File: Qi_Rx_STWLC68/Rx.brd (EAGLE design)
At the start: 160 x 100 mm, 44 parts, among them IC1 STWLC68JRH

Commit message: Complete SMD layout
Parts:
- moved R3 44.7 mm to (11.4, 15.2)
- moved R4 43.7 mm to (15.2, 15.2)
- moved R5 42.7 mm to (19.1, 15.2)
- moved C11 40.7 mm to (34.3, 19.1)
- moved C7 40.7 mm to (39.4, 12.7)
- moved C8 40.7 mm to (34.3, 12.7)
- moved C9 40.7 mm to (39.4, 19.1)
- moved U$2 40.7 mm to (48.3, 21.6)
- moved C1 40.7 mm to (39.4, 8.89)
- moved C10 40.7 mm to (36.8, 19.1)
- moved C12 40.7 mm to (43.2, 26.7)
- moved C13 40.7 mm to (25.4, 8.89)
- moved C14 40.7 mm to (22.9, 8.89)
- moved C15 40.7 mm to (40.6, 26.7)
- moved C17 40.7 mm to (35.6, 26.7)
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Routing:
- net VOUT: track 14.1 -> 37.1 mm
- net SDA: track 29.9 -> 33.7 mm
- net INT: track 27.1 -> 29.6 mm
- net GND: vias 0 -> 21
- added copper zone on layer 1, net GND
- added copper zone on layer 15, net GND
- added copper zone on layer 16, net GND
- added copper zone on layer 2, net GND
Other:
- board size 160 x 100 mm -> 68.6 x 38.1 mm

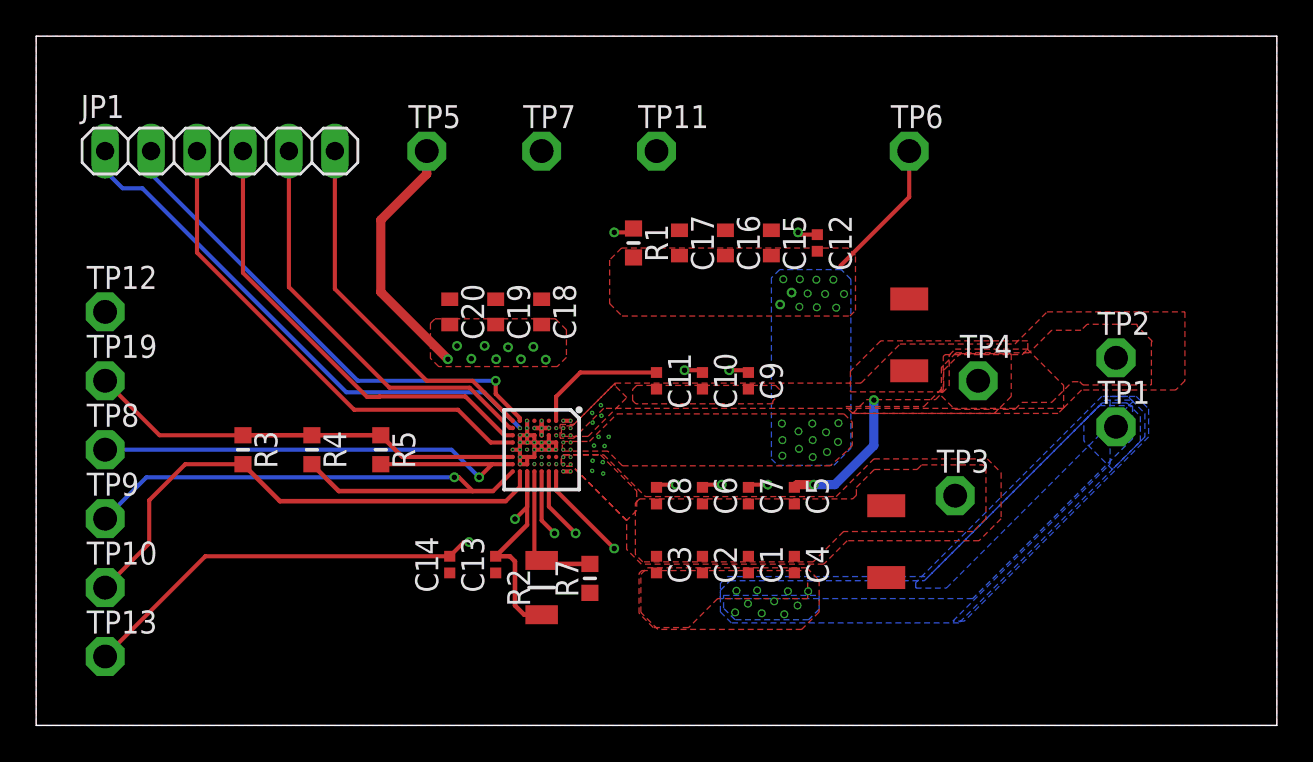
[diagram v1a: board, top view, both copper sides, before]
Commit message: Rx surface-mount cleanup
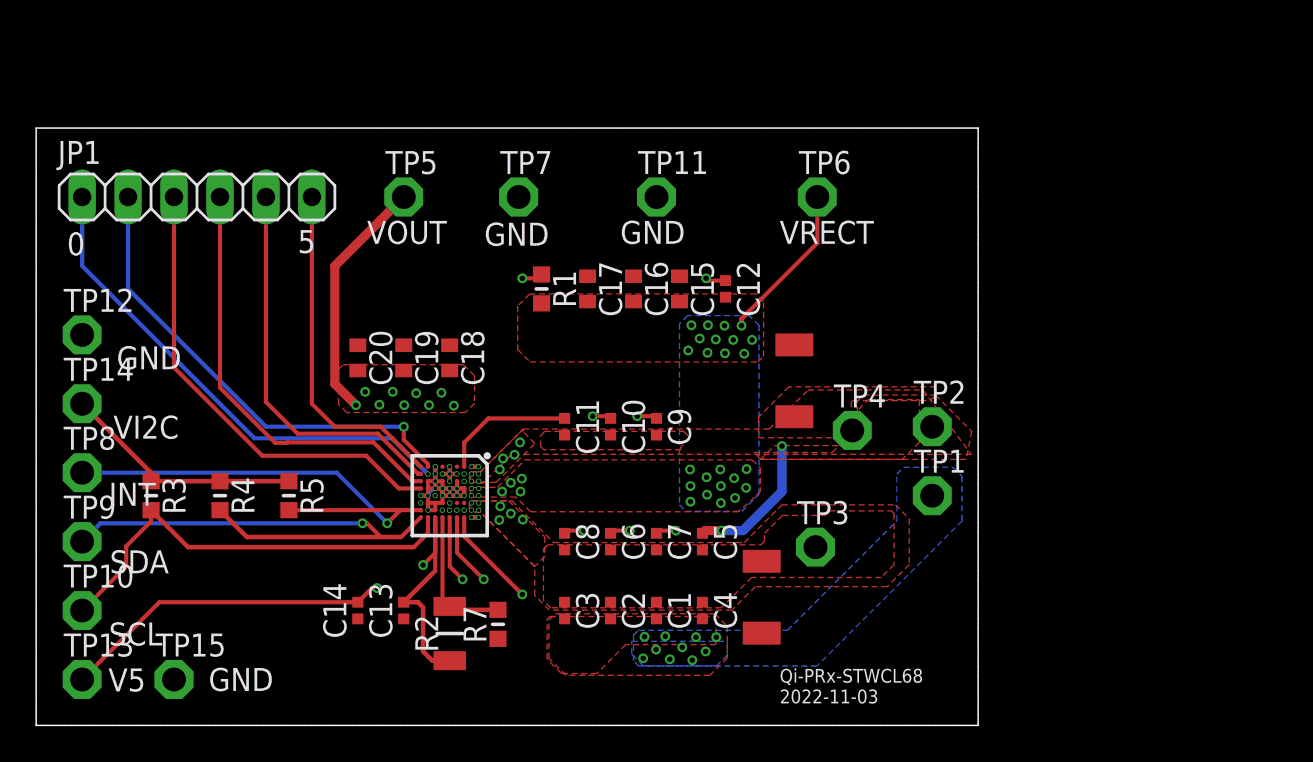
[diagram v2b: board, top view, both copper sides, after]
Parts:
- removed TP19: PTR1PAD1-13, testpad:P1-13
- added TP14, TP15: TPPAD1-13, testpad:P1-13
- moved TP1 10.9 mm to (49.5, 12.7)
- moved TP2 10.9 mm to (49.5, 16.5)
- moved TP3 8.23 mm to (43.1, 9.86)
- moved U$1 7.54 mm to (40.1, 7.09)
- moved TP4 7.48 mm to (45.1, 16.3)
- moved U$2 6.84 mm to (41.9, 19.1)
- moved C17 5.68 mm to (30.5, 24.1)
- moved R1 5.68 mm to (27.9, 24.1)
- moved IC1 5.68 mm to (22.9, 12.7)
- moved C18 5.68 mm to (22.9, 20.3)
- moved R2 5.68 mm to (22.9, 5.08)
- moved R3 5.68 mm to (6.35, 12.7)
- moved R4 5.68 mm to (10.2, 12.7)
- moved R5 5.68 mm to (14.0, 12.7)
- moved C1 5.68 mm to (34.3, 6.35)
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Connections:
- new net VI2C: R3.2, R4.2, R5.2, TP14.TP
- net GND: now also TP15.TP
- net V18: no longer R3.2, R4.2, R5.2, TP19.TP
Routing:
- net V18: track 42.0 -> 19.7 mm, vias 2 -> 3
- net GND: track 12.4 -> 30.1 mm, vias 21 -> 18
- net VI2C: track 0.00 -> 13.5 mm
- net SCL: track 29.2 -> 24.5 mm
- net SDA: track 33.7 -> 29.4 mm
- net V5: track 30.8 -> 26.5 mm
- net INT: track 29.6 -> 26.3 mm
- net GPIO0: track 29.9 -> 27.7 mm
- net VOUT: track 37.1 -> 39.2 mm
- net GPIO5: track 20.5 -> 18.9 mm
- net GPIO1: track 27.8 -> 26.2 mm
- net GPIO4: track 23.1 -> 21.5 mm
- net GPIO3: track 25.4 -> 23.8 mm
- net GPIO2: track 27.4 -> 25.8 mm
- net VRECT: track 8.54 -> 9.50 mm
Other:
- board size 68.6 x 38.1 mm -> 52.1 x 33 mm
- board text added: "0"
- board text added: "5"
- board text added: "GND"
- board text added: "INT"
- board text added: "Qi-PRx-STWCL68 2022-11-03"
- board text added: "SCL"
- board text added: "SDA"
- board text added: "V5"
- board text added: "VI2C"
- board text added: "VOUT"
- board text added: "VRECT"
